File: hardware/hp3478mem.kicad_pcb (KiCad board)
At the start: 2 copper layers, 12.3 x 28.6 mm, 9 parts, among them J1 uPD5101LC, J2 PROG_HDR, U1 ATtiny406

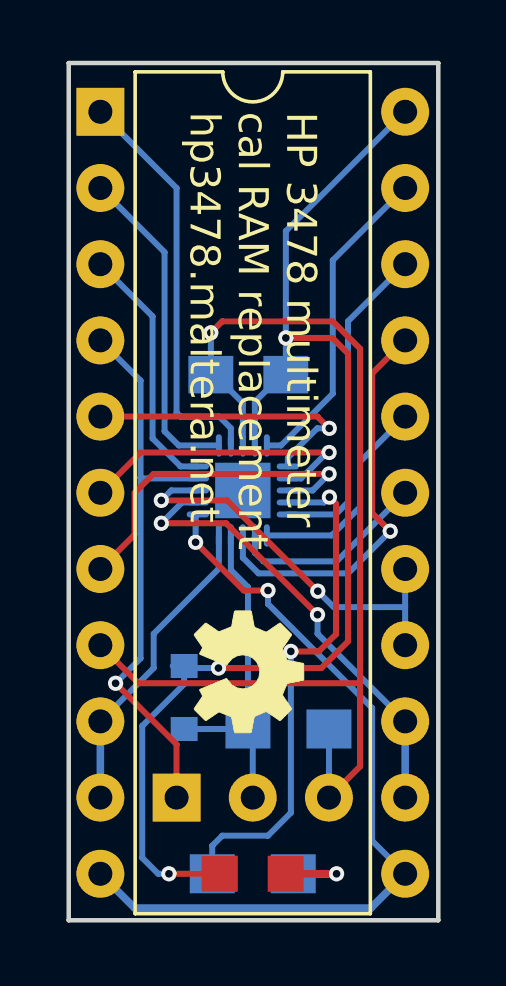
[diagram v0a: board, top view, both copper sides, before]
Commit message: Update pad sizes based on issues with prototypes.
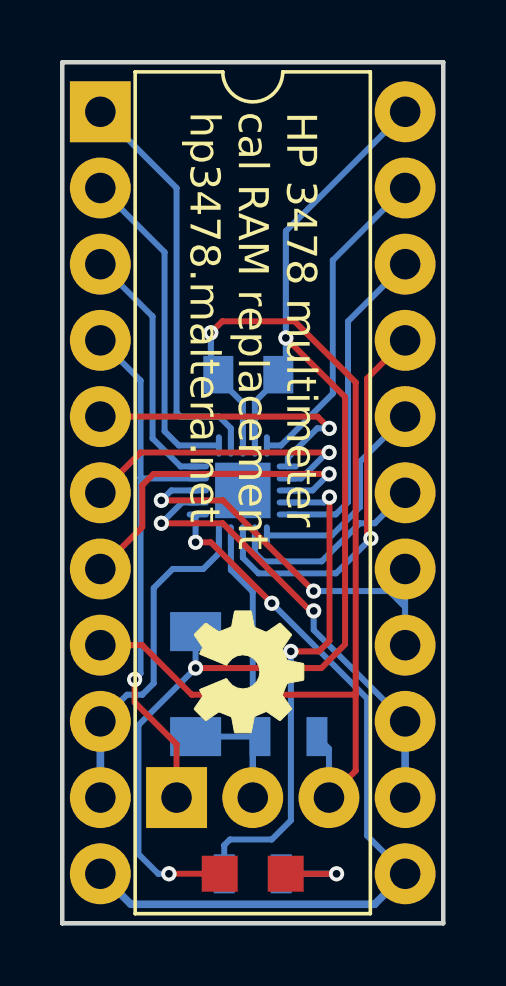
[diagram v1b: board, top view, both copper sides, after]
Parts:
- C1: footprint Capacitors_SMD:C_0805_HandSoldering -> Capacitors_SMD:C_0805
- D2: footprint Diodes_SMD:D_0805 -> Diodes_SMD:D_MiniMELF
- R1: value 100R -> 470R; footprint Resistors_SMD:R_0805_HandSoldering -> Resistors_SMD:R_0805
- R2: value 1k -> 4k7; footprint Resistors_SMD:R_0805_HandSoldering -> Resistors_SMD:R_0805
- moved D2 0.59 mm to (104.8, 120.7)
- moved R2 0.25 mm to (107.9, 122.4)
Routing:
- net /PS: track 11.7 -> 13.3 mm
- net GND: track 36.9 -> 35.7 mm
- net /D1: track 10.4 -> 11.3 mm
- net /~CE1: track 13.5 -> 12.9 mm
- net /A0: track 18.9 -> 18.4 mm
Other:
- board size 12.3 x 28.6 mm -> 12.7 x 28.7 mm
- rule pad_to_mask_clearance: 0.2 -> 0.0508

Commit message: Add more silkscreen labels.
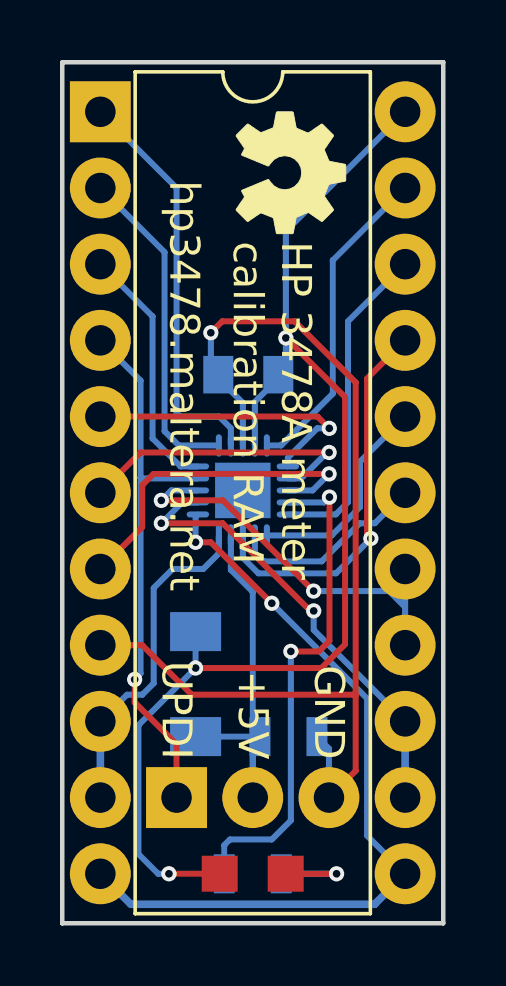
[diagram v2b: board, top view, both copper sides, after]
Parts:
- moved OSHW 16.7 mm to (108.0, 103.6)
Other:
- board text added: "+5V"
- board text added: "GND"
- board text added: "HP 3478A meter calibration RAM"
- board text added: "UPDI"
- board text added: "hp3478.maltera.net"
- board text removed: "HP 3478 multimeter cal RAM replacement hp3478.maltera.net"
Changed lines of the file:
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@@
     (area 100.254999 99.873999 113.105001 128.726001)
     (thickness 1.6)
-    (drawings 5)
+    (drawings 9)
     (tracks 171)
     (zones 0)
@@
     (35 F.Paste user)
     (36 B.SilkS user)
-    (37 F.SilkS user hide)
+    (37 F.SilkS user)
     (38 B.Mask user)
     (39 F.Mask user)
@@
   )
   (module custom:OSHW (layer F.Cu)
-    (at 106.553 120.269 270)
+    (at 107.95 103.632 270)
     (descr "Imported from /home/sam/Downloads/oshw.svg")
     (tags svg2mod)
@@
     )
   )
-  (gr_text "HP 3478 multimeter\ncal RAM replacement\nhp3478.maltera.net" (at 106.68 101.6 270) (layer F.SilkS)
+  (gr_text "HP 3478A meter\ncalibration RAM\n" (at 107.315 105.918 270) (layer F.SilkS)
     (effects (font (size 1 1) (thickness 0.15)) (justify left))
   )
+  (gr_text UPDI (at 104.14 123.19 270) (layer F.SilkS)
+    (effects (font (size 1 1) (thickness 0.15)) (justify right))
+  )
+  (gr_text +5V (at 106.68 123.19 270) (layer F.SilkS)
+    (effects (font (size 1 1) (thickness 0.15)) (justify right))
+  )
+  (gr_text GND (at 109.22 123.19 270) (layer F.SilkS)
+    (effects (font (size 1 1) (thickness 0.15)) (justify right))
+  )
+  (gr_text "hp3478.maltera.net\n" (at 104.394 103.886 270) (layer F.SilkS)
+    (effects (font (size 1 1) (thickness 0.15)) (justify left))
+  )
